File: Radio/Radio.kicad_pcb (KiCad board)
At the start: 2 copper layers, 30 x 43.8 mm, 15 parts, among them J1 USB_B_Micro, J2 Conn_Coaxial, U1 FT231XS, U2 XB3

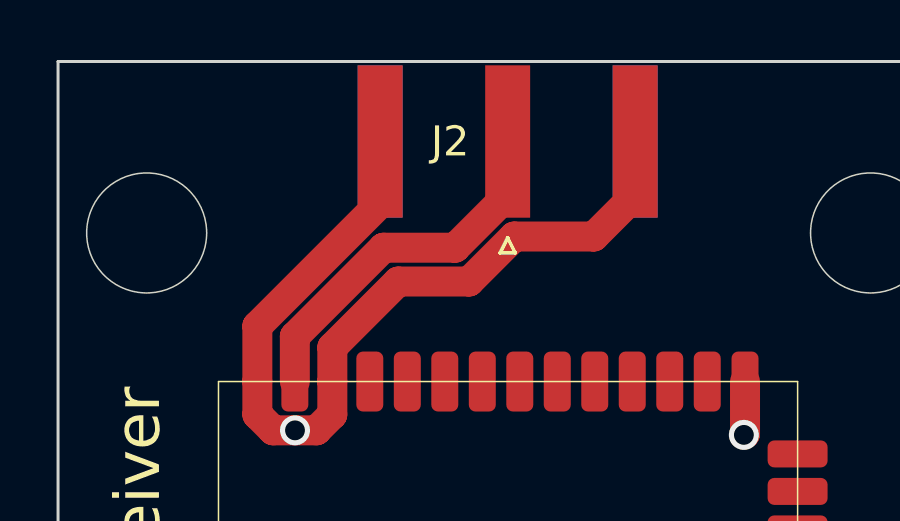
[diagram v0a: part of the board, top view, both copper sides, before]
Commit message: Shrank RP-SMA footprint
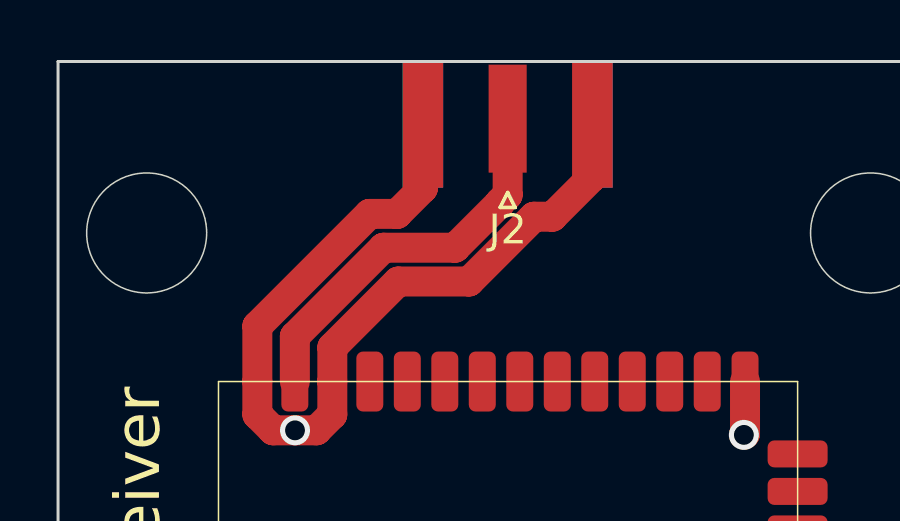
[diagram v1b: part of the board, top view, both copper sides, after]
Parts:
- J2: footprint Connector_Coaxial:SMA_Amphenol_132289_EdgeMount -> Connector_Coaxial:SMA_Samtec_SMA-J-P-H-ST-EM1_EdgeMount
- moved J2 0.56 mm to (150.0, 68.3)
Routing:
- net Net-(J2-Pad1): track 12.3 -> 13.1 mm

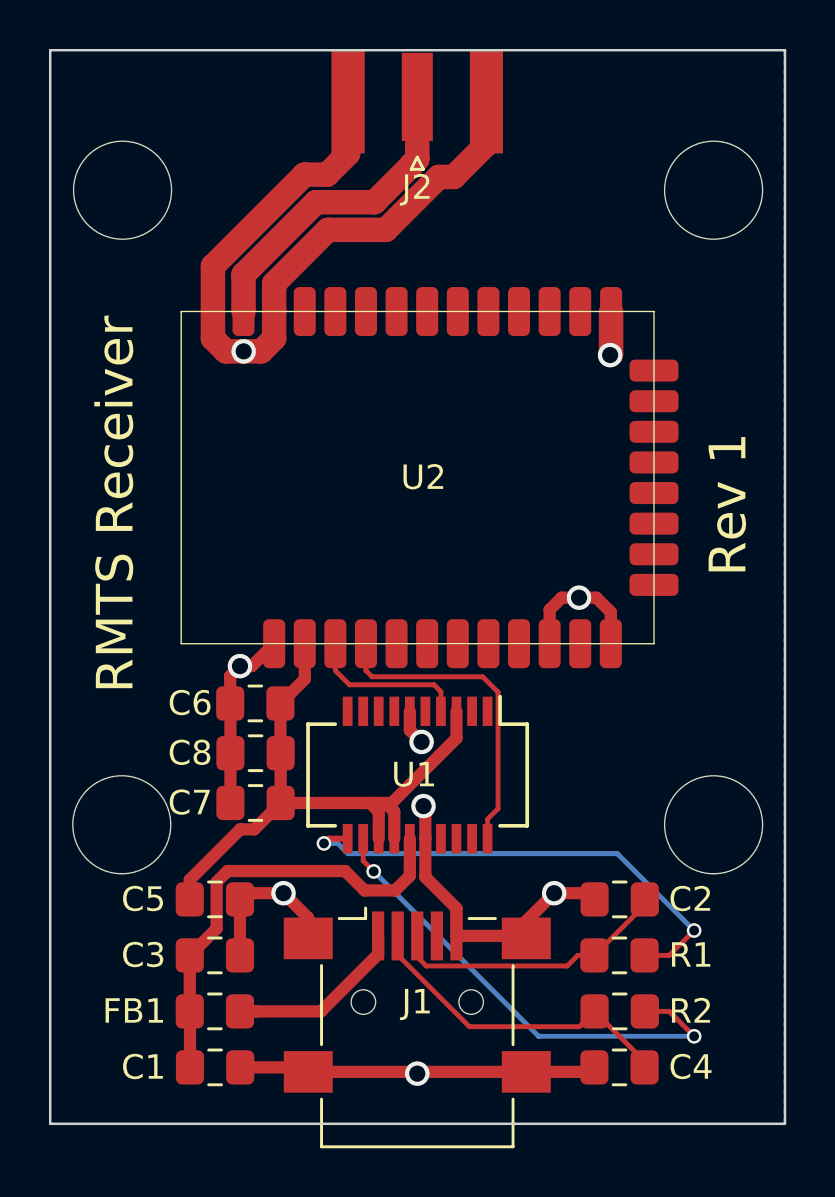
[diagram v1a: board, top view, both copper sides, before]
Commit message: Add silkscreen rectangle for SN, reduce mounting hole size
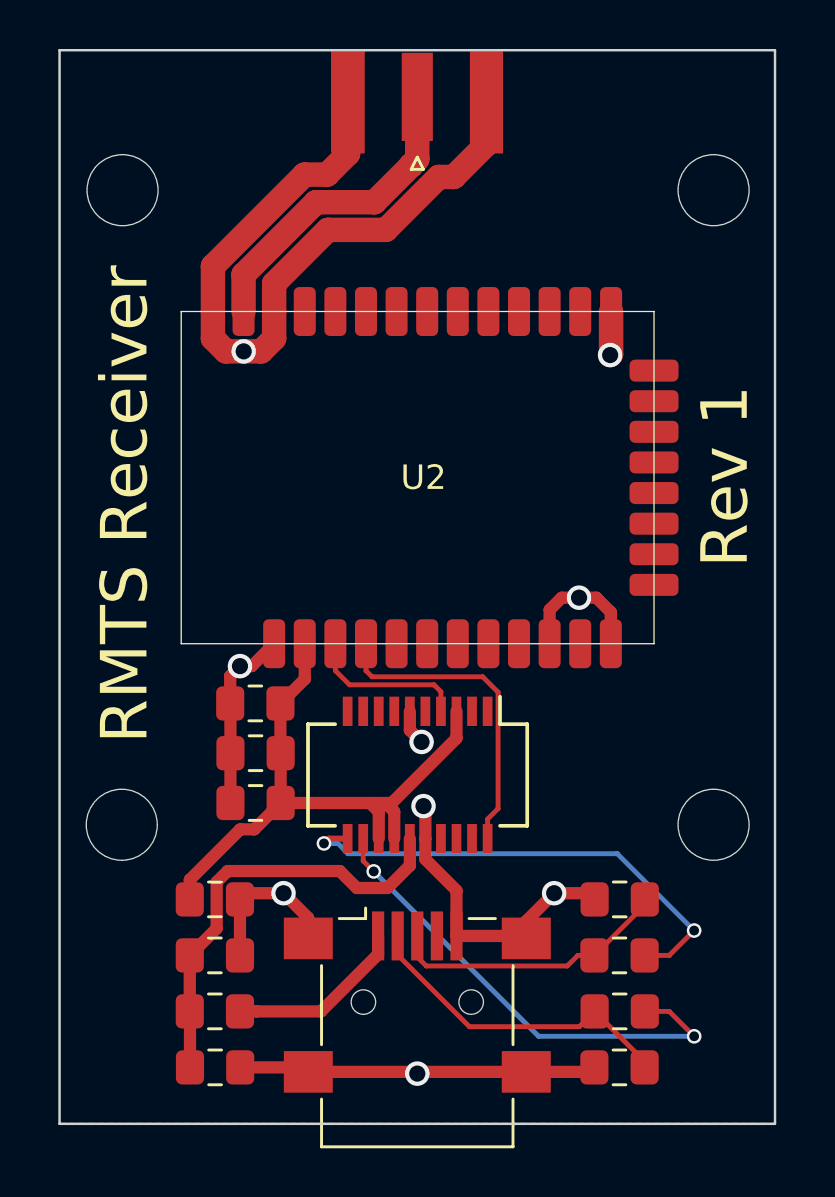
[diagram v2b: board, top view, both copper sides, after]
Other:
- board size 30 x 43.8 mm -> 29.2 x 43.8 mm
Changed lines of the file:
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@@
   (general
     (thickness 1.6)
-    (drawings 10)
-    (tracks 165)
+    (drawings 11)
+    (tracks 164)
     (zones 0)
     (modules 15)
@@
   )
   (setup
-    (last_trace_width 1)
+    (last_trace_width 0.5)
     (user_trace_width 0.5)
     (user_trace_width 1)
@@
       (outputformat 1)
       (mirror false)
-      (drillshape 1)
+      (drillshape 0)
       (scaleselection 1)
-      (outputdirectory ""))
+      (outputdirectory "../../Radio Rev 1 Gerber/"))
   )
   (net 0 "")
@@
     (tags SMA)
     (attr smd)
-    (fp_text reference J2 (at -3.5 0) (layer F.SilkS)
+    (fp_text reference J2 (at -3.5 0) (layer F.SilkS) hide
       (effects (font (size 1 1) (thickness 0.15)))
     )
@@
     (tags "capacitor handsolder")
     (attr smd)
-    (fp_text reference C8 (at 2.667 0) (layer F.SilkS)
+    (fp_text reference C8 (at 2.667 0) (layer F.SilkS) hide
       (effects (font (size 1 1) (thickness 0.15)))
     )
@@
     (tags "capacitor handsolder")
     (attr smd)
-    (fp_text reference C7 (at 2.667 0) (layer F.SilkS)
+    (fp_text reference C7 (at 2.667 0) (layer F.SilkS) hide
       (effects (font (size 1 1) (thickness 0.15)))
     )
@@
     (tags "resistor handsolder")
     (attr smd)
-    (fp_text reference R2 (at -2.912 0) (layer F.SilkS)
+    (fp_text reference R2 (at -2.912 0) (layer F.SilkS) hide
       (effects (font (size 1 1) (thickness 0.15)))
     )
@@
     (tags "resistor handsolder")
     (attr smd)
-    (fp_text reference R1 (at -2.921 0) (layer F.SilkS)
+    (fp_text reference R1 (at -2.921 0) (layer F.SilkS) hide
       (effects (font (size 1 1) (thickness 0.15)))
     )
@@
     (tags "USB USB_B USB_Mini connector")
     (attr smd)
-    (fp_text reference J1 (at 0 0) (layer F.SilkS)
+    (fp_text reference J1 (at 0 0) (layer F.SilkS) hide
       (effects (font (size 1 1) (thickness 0.15)))
     )
@@
     (tags "capacitor handsolder")
     (attr smd)
-    (fp_text reference FB1 (at -3.293 0) (layer F.SilkS)
+    (fp_text reference FB1 (at -3.293 0) (layer F.SilkS) hide
       (effects (font (size 1 1) (thickness 0.15)))
     )
@@
     (tags "capacitor handsolder")
     (attr smd)
-    (fp_text reference C6 (at 2.658 0) (layer F.SilkS)
+    (fp_text reference C6 (at 2.658 0) (layer F.SilkS) hide
       (effects (font (size 1 1) (thickness 0.15)))
     )
@@
     (tags "capacitor handsolder")
     (attr smd)
-    (fp_text reference C5 (at -2.912 0) (layer F.SilkS)
+    (fp_text reference C5 (at -2.912 0) (layer F.SilkS) hide
       (effects (font (size 1 1) (thickness 0.15)))
     )
@@
     (tags "capacitor handsolder")
     (attr smd)
-    (fp_text reference C4 (at -2.921 0) (layer F.SilkS)
+    (fp_text reference C4 (at -2.921 0) (layer F.SilkS) hide
       (effects (font (size 1 1) (thickness 0.15)))
     )
@@
     (tags "capacitor handsolder")
     (attr smd)
-    (fp_text reference C3 (at -2.912 0) (layer F.SilkS)
+    (fp_text reference C3 (at -2.912 0) (layer F.SilkS) hide
       (effects (font (size 1 1) (thickness 0.15)))
     )
@@
     (tags "capacitor handsolder")
     (attr smd)
-    (fp_text reference C2 (at -2.912 0) (layer F.SilkS)
+    (fp_text reference C2 (at -2.912 0) (layer F.SilkS) hide
       (effects (font (size 1 1) (thickness 0.15)))
     )
@@
     (tags "capacitor handsolder")
     (attr smd)
-    (fp_text reference C1 (at -2.921 0) (layer F.SilkS)
+    (fp_text reference C1 (at -2.921 0) (layer F.SilkS) hide
       (effects (font (size 1 1) (thickness 0.15)))
     )
@@
     (tags "SSOP 0.635")
     (attr smd)
-    (fp_text reference U1 (at 0 0.14 180) (layer F.SilkS)
+    (fp_text reference U1 (at 0 0.14 180) (layer F.SilkS) hide
       (effects (font (size 1 1) (thickness 0.15)))
     )
@@
     )
   )
-  (gr_text "Rev 1" (at 162.687 84.709 90) (layer F.SilkS)
-    (effects (font (size 1.5 1.5) (thickness 0.3)))
-  )
-  (gr_text "RMTS Receiver" (at 137.668 84.709 90) (layer F.SilkS)
-    (effects (font (size 1.5 1.5) (thickness 0.3)))
-  )
-  (gr_circle (center 162.084 97.79) (end 164.084 97.79) (layer Edge.Cuts) (width 0.05))
-  (gr_circle (center 137.922 97.79) (end 139.922 97.79) (layer Edge.Cuts) (width 0.05))
-  (gr_circle (center 162.084 71.882) (end 164.084 71.882) (layer Edge.Cuts) (width 0.05))
-  (gr_circle (center 137.954 71.882) (end 139.954 71.882) (layer Edge.Cuts) (width 0.05))
-  (gr_line (start 135 110) (end 135 66.167) (layer Edge.Cuts) (width 0.1))
-  (gr_line (start 165 110) (end 135 110) (layer Edge.Cuts) (width 0.1))
-  (gr_line (start 165 66.167) (end 165 110) (layer Edge.Cuts) (width 0.1))
-  (gr_line (start 135 66.167) (end 165 66.167) (layer Edge.Cuts) (width 0.1))
+  (gr_poly (pts (xy 138.303 80.391) (xy 138.303 86.868) (xy 161.671 86.868) (xy 161.671 80.391)) (layer B.SilkS) (width 0.1))
+  (gr_text "Rev 1" (at 162.56 83.566 90) (layer F.SilkS)
+    (effects (font (size 1.9 1.9) (thickness 0.35)))
+  )
+  (gr_text "RMTS Receiver" (at 138.049 84.709 90) (layer F.SilkS)
+    (effects (font (size 1.9 1.9) (thickness 0.35)))
+  )
+  (gr_circle (center 162.084 97.79) (end 163.534 97.79) (layer Edge.Cuts) (width 0.05))
+  (gr_circle (center 137.922 97.79) (end 139.372 97.79) (layer Edge.Cuts) (width 0.05))
+  (gr_circle (center 162.084 71.882) (end 163.534 71.882) (layer Edge.Cuts) (width 0.05))
+  (gr_circle (center 137.954 71.882) (end 139.404 71.882) (layer Edge.Cuts) (width 0.05))
+  (gr_line (start 135.382 110) (end 135.382 66.167) (layer Edge.Cuts) (width 0.1))
+  (gr_line (start 164.592 110) (end 135.382 110) (layer Edge.Cuts) (width 0.1))
+  (gr_line (start 164.592 66.167) (end 164.592 110) (layer Edge.Cuts) (width 0.1))
+  (gr_line (start 135.382 66.167) (end 164.592 66.167) (layer Edge.Cuts) (width 0.1))
   (segment (start 149.804 107.879) (end 149.733 107.95) (width 0.25) (layer F.Cu) (net 1))
   (segment (start 144.842 103.124) (end 145.537 102.429) (width 0.25) (layer F.Cu) (net 1))
@@
   (segment (start 157.034 107.879) (end 157.217 107.696) (width 0.5) (layer F.Cu) (net 1))
   (segment (start 154.437 107.879) (end 157.034 107.879) (width 0.5) (layer F.Cu) (net 1))
-  (segment (start 151.587 101.200398) (end 151.587 102.329) (width 0.5) (layer F.Cu) (net 1))
-  (segment (start 150.3175 99.930898) (end 151.587 101.200398) (width 0.5) (layer F.Cu) (net 1))
-  (segment (start 150.3175 98.358) (end 150.3175 99.930898) (width 0.5) (layer F.Cu) (net 1))
   (segment (start 154.337 102.329) (end 154.437 102.429) (width 0.5) (layer F.Cu) (net 1))
   (segment (start 151.587 102.329) (end 154.337 102.329) (width 0.5) (layer F.Cu) (net 1))
@@
   (segment (start 147.162 70.389) (end 147.162 68.272) (width 1) (layer F.Cu) (net 1))
   (segment (start 146.30401 71.24699) (end 147.162 70.389) (width 1) (layer F.Cu) (net 1))
+  (segment (start 151.587 100.471102) (end 151.587 102.329) (width 0.5) (layer F.Cu) (net 1))
+  (segment (start 150.3175 98.358) (end 150.3175 99.201602) (width 0.5) (layer F.Cu) (net 1))
+  (segment (start 150.3175 99.201602) (end 151.587 100.471102) (width 0.5) (layer F.Cu) (net 1))
   (segment (start 145.39244 91.84356) (end 144.399 92.837) (width 0.5) (layer F.Cu) (net 2))
   (segment (start 145.39244 90.3986) (end 145.39244 91.84356) (width 0.5) (layer F.Cu) (net 2))
@@
   (segment (start 140.707 107.696) (end 140.707 105.419) (width 0.5) (layer F.Cu) (net 6))
   (segment (start 140.698 105.41) (end 140.698 103.124) (width 0.5) (layer F.Cu) (net 6))
-  (segment (start 149.6825 99.458) (end 149.6825 98.358) (width 0.5) (layer F.Cu) (net 6))
-  (segment (start 149.6825 99.8725) (end 149.6825 99.458) (width 0.5) (layer F.Cu) (net 6))
-  (segment (start 147.836039 100.472001) (end 149.082999 100.472001) (width 0.5) (layer F.Cu) (net 6))
-  (segment (start 142.244273 99.679999) (end 147.044037 99.679999) (width 0.5) (layer F.Cu) (net 6))
-  (segment (start 149.082999 100.472001) (end 149.6825 99.8725) (width 0.5) (layer F.Cu) (net 6))
   (segment (start 141.79599 100.128282) (end 142.244273 99.679999) (width 0.5) (layer F.Cu) (net 6))
-  (segment (start 147.044037 99.679999) (end 147.836039 100.472001) (width 0.5) (layer F.Cu) (net 6))
   (segment (start 141.79599 102.02601) (end 141.79599 100.128282) (width 0.5) (layer F.Cu) (net 6))
   (segment (start 140.698 103.124) (end 141.79599 102.02601) (width 0.5) (layer F.Cu) (net 6))
+  (segment (start 147.519003 100.372001) (end 146.827001 99.679999) (width 0.5) (layer F.Cu) (net 6))
+  (segment (start 148.768499 100.372001) (end 147.519003 100.372001) (width 0.5) (layer F.Cu) (net 6))
+  (segment (start 149.6825 99.458) (end 148.768499 100.372001) (width 0.5) (layer F.Cu) (net 6))
+  (segment (start 149.6825 98.358) (end 149.6825 99.458) (width 0.5) (layer F.Cu) (net 6))
+  (segment (start 142.244273 99.679999) (end 146.827001 99.679999) (width 0.5) (layer F.Cu) (net 6))
   (segment (start 148.209 99.695) (end 154.051 105.537) (width 0.2) (layer B.Cu) (net 7))
   (segment (start 147.7775 99.2635) (end 147.7775 98.358) (width 0.2) (layer F.Cu) (net 7))
@@
     (polygon
       (pts
-        (xy 164.973 71.882) (xy 164.973 66.167) (xy 135.001 66.167) (xy 135.001 109.982) (xy 164.973 109.982)
+        (xy 164.592 72.009) (xy 164.592 66.167) (xy 135.382 66.167) (xy 135.382 109.982) (xy 164.592 109.982)
       )
     )
